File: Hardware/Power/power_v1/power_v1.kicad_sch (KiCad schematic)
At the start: 34 parts, among them J1 Conn_01x03, Q1 SIHF9Z24STRR-GE3, U1 LM3940, U2 SI-8050Y

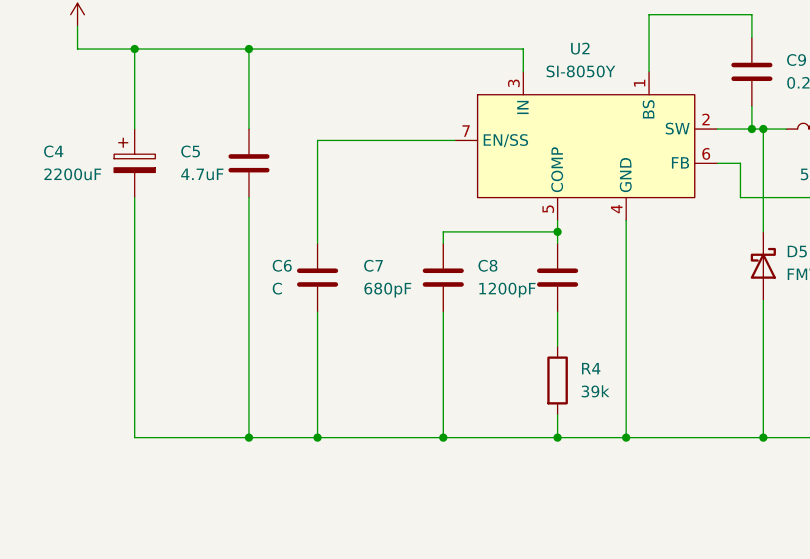
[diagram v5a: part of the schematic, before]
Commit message: fixed C6 and F1, chose L1 part and created footprint for it
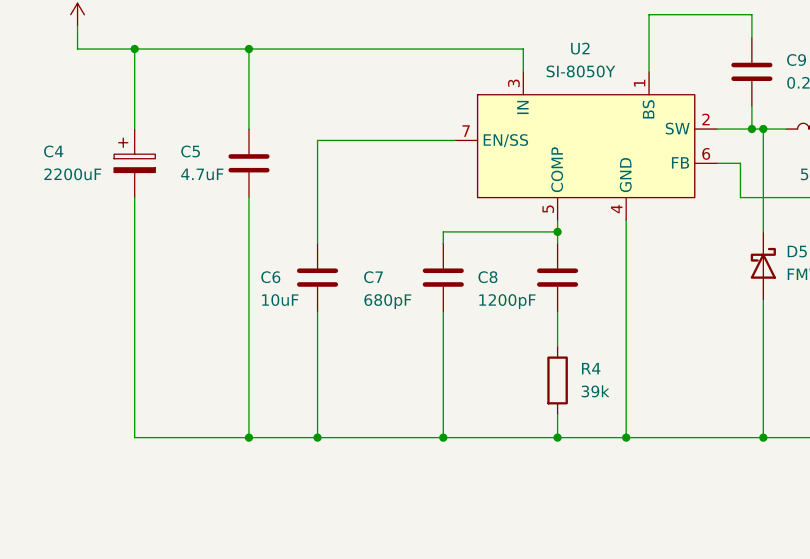
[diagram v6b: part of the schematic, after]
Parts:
- C6: value C -> 10uF; footprint (none) -> Capacitor_SMD:C_0805_2012Metric_Pad1.18x1.45mm_HandSolder; MPN (none) -> CAP CER 10UF 25V X5R 0805; Stock (none) -> https://www.digikey.com/en/products/detail/kyocera-avx/0805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
- F1: footprint (none) -> Fuse:Fuse_0603_1608Metric_Pad1.05x0.95mm_HandSolder; MPN (none) -> SF-0603SPA500R-2; Stock (none) -> https://www.mouser.com/ProductDetail/Bourns/SF-0603SPA500R-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
- L1: footprint (none) -> BackpackBuddyFootprintLibrary:Inductor_IHLP6767GZER560M11; MPN (none) -> FIXED IND 56UH 7.2A 57.8MOHM SMD; Stock (none) -> https://www.digikey.com/en/products/detail/vishay-dale/IHLP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
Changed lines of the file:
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@@
   (symbol (lib_id "Device:C") (at 95.25 146.05 0) (unit 1)
     (in_bom yes) (on_board yes)
-    (property "Reference" "C8" (id 0) (at 86.36 144.78 0)
-      (effects (font (size 1.27 1.27)) (justify left))
-    )
-    (property "Value" "1200pF" (id 1) (at 86.36 147.32 0)
+    (property "Reference" "C8" (id 0) (at 86.36 146.05 0)
+      (effects (font (size 1.27 1.27)) (justify left))
+    )
+    (property "Value" "1200pF" (id 1) (at 86.36 148.59 0)
       (effects (font (size 1.27 1.27)) (justify left))
     )
@@
   (symbol (lib_id "Device:C") (at 82.55 146.05 0) (unit 1)
     (in_bom yes) (on_board yes)
-    (property "Reference" "C7" (id 0) (at 73.66 144.78 0)
-      (effects (font (size 1.27 1.27)) (justify left))
-    )
-    (property "Value" "680pF" (id 1) (at 73.66 147.32 0)
+    (property "Reference" "C7" (id 0) (at 73.66 146.05 0)
+      (effects (font (size 1.27 1.27)) (justify left))
+    )
+    (property "Value" "680pF" (id 1) (at 73.66 148.59 0)
       (effects (font (size 1.27 1.27)) (justify left))
     )
@@
   (symbol (lib_id "Device:C") (at 68.58 146.05 0) (unit 1)
     (in_bom yes) (on_board yes)
-    (property "Reference" "C6" (id 0) (at 63.5 144.78 0)
-      (effects (font (size 1.27 1.27)) (justify left))
-    )
-    (property "Value" "C" (id 1) (at 63.5 147.32 0)
-      (effects (font (size 1.27 1.27)) (justify left))
-    )
-    (property "Footprint" "" (id 2) (at 69.5452 149.86 0)
+    (property "Reference" "C6" (id 0) (at 62.23 146.05 0)
+      (effects (font (size 1.27 1.27)) (justify left))
+    )
+    (property "Value" "10uF" (id 1) (at 62.23 148.59 0)
+      (effects (font (size 1.27 1.27)) (justify left))
+    )
+    (property "Footprint" "Capacitor_SMD:C_0805_2012Metric_Pad1.18x1.45mm_HandSolder" (id 2) (at 69.5452 149.86 0)
       (effects (font (size 1.27 1.27)) hide)
     )
     (property "Datasheet" "~" (id 3) (at 68.58 146.05 0)
+      (effects (font (size 1.27 1.27)) hide)
+    )
+    (property "MPN" "CAP CER 10UF 25V X5R 0805" (id 4) (at 68.58 146.05 0)
+      (effects (font (size 1.27 1.27)) hide)
+    )
+    (property "Stock" "https://www.digikey.com/en/products/detail/kyocera-avx/08053D106KAT4A/12153448?utm_adgroup=Capacitors&utm_source=google&utm_medium=cpc&utm_campaign=Shopping_Supplier_AVX%20Corporation&utm_term=&utm_content=Capacitors" (id 5) (at 68.58 146.05 0)
       (effects (font (size 1.27 1.27)) hide)
     )
@@
     (property "Reference" "L1" (id 0) (at 124.46 132.08 90))
     (property "Value" "56uH" (id 1) (at 124.46 134.62 90))
-    (property "Footprint" "" (id 2) (at 124.46 129.54 0)
-      (effects (font (size 1.27 1.27)) hide)
-    )
-    (property "Datasheet" "~" (id 3) (at 124.46 129.54 0)
+    (property "Footprint" "BackpackBuddyFootprintLibrary:Inductor_IHLP6767GZER560M11" (id 2) (at 124.46 129.54 0)
+      (effects (font (size 1.27 1.27)) hide)
+    )
+    (property "Datasheet" "https://www.vishay.com/docs/34282/ihlp-6767gz-11.pdf" (id 3) (at 124.46 129.54 0)
+      (effects (font (size 1.27 1.27)) hide)
+    )
+    (property "Stock" "https://www.digikey.com/en/products/detail/vishay-dale/IHLP6767GZER560M11/2139396" (id 4) (at 124.46 129.54 0)
+      (effects (font (size 1.27 1.27)) hide)
+    )
+    (property "MPN" "FIXED IND 56UH 7.2A 57.8MOHM SMD" (id 5) (at 124.46 129.54 0)
       (effects (font (size 1.27 1.27)) hide)
     )
@@
     (property "Reference" "F1" (id 0) (at 69.85 31.75 90))
     (property "Value" "4A" (id 1) (at 69.85 34.29 90))
-    (property "Footprint" "" (id 2) (at 69.85 39.878 90)
-      (effects (font (size 1.27 1.27)) hide)
-    )
-    (property "Datasheet" "~" (id 3) (at 69.85 38.1 0)
+    (property "Footprint" "Fuse:Fuse_0603_1608Metric_Pad1.05x0.95mm_HandSolder" (id 2) (at 69.85 39.878 90)
+      (effects (font (size 1.27 1.27)) hide)
+    )
+    (property "Datasheet" "https://www.mouser.com/datasheet/2/54/Bourns_SF_0603SPA_R_datasheet-2935204.pdf" (id 3) (at 69.85 38.1 0)
+      (effects (font (size 1.27 1.27)) hide)
+    )
+    (property "MPN" "SF-0603SPA500R-2" (id 4) (at 69.85 38.1 0)
+      (effects (font (size 1.27 1.27)) hide)
+    )
+    (property "Stock" "https://www.mouser.com/ProductDetail/Bourns/SF-0603SPA500R-2?qs=sGAEpiMZZMsIz3CjQ1xegZx2pdJYlyprauhgMChWNHkdzemHf%2F5IKw%3D%3D" (id 5) (at 69.85 38.1 0)
       (effects (font (size 1.27 1.27)) hide)
     )
@@
     )
     (path "/950d0414-a84a-4032-b67c-e2903ea70539"
-      (reference "C6") (unit 1) (value "C") (footprint "")
+      (reference "C6") (unit 1) (value "10uF") (footprint "Capacitor_SMD:C_0805_2012Metric_Pad1.18x1.45mm_HandSolder")
     )
     (path "/6984617a-3785-498d-8bc3-b2e734f45901"
@@
     )
     (path "/d5f8468c-3f8c-4ea7-89be-5df8ca042e00"
-      (reference "F1") (unit 1) (value "4A") (footprint "")
+      (reference "F1") (unit 1) (value "4A") (footprint "Fuse:Fuse_0603_1608Metric_Pad1.05x0.95mm_HandSolder")
     )
     (path "/002442d1-da6c-4fcd-9a5b-91926eead4c3"
@@
     )
     (path "/b957d33e-791c-4070-bbf2-9fac75b1e692"
-      (reference "L1") (unit 1) (value "56uH") (footprint "")
+      (reference "L1") (unit 1) (value "56uH") (footprint "BackpackBuddyFootprintLibrary:Inductor_IHLP6767GZER560M11")
     )
     (path "/d7983cbf-b99b-429c-9a4e-ae33e2b5964e"
